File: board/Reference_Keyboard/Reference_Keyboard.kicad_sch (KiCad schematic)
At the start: 76 parts, among them J1 Conn_01x03_Pin, J2 USB_C_Receptacle_USB2.0, J3 Conn_01x04_Pin, J4 84953-4, SW1 SW_Push, SW10 SW_Push, SW11 SW_Push, SW12 SW_Push, SW13 SW_Push, SW14 SW_Push, SW15 SW_Push, SW16 SW_Push, SW17 SW_Push, SW18 SW_Push, SW19 SW_Push, SW2 SW_Push, SW20 SW_Push, SW21 SW_Push, SW22 SKQGAFE010, SW23 SKQGAFE010, SW24 RotaryEncoder_Switch, SW3 SW_Push, SW4 SW_Push, SW5 SW_Push, SW6 SW_Push, SW7 SW_Push, SW8 SW_Push, SW9 SW_Push, U1 RP2040, U2 W25Q16JVSSIM, U3 LM1117RS-3.3, Y1 NX3225SA-12MHz-STD-CSR-6

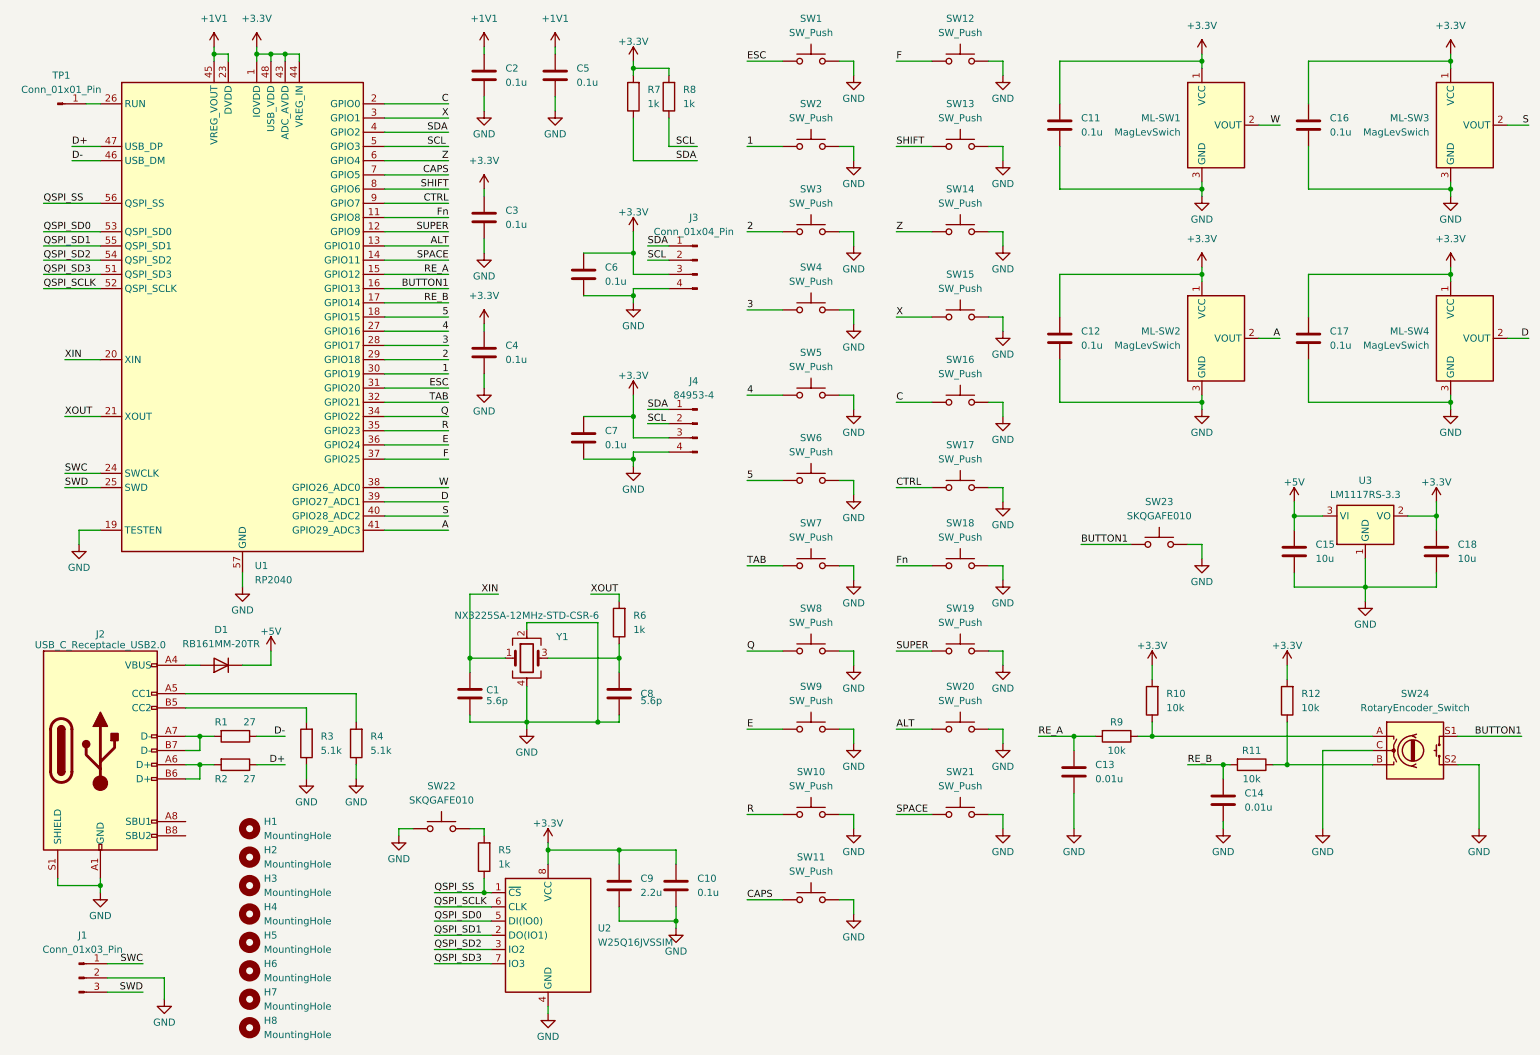
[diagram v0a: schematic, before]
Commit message: add firmware and PCB for hardware v1.01
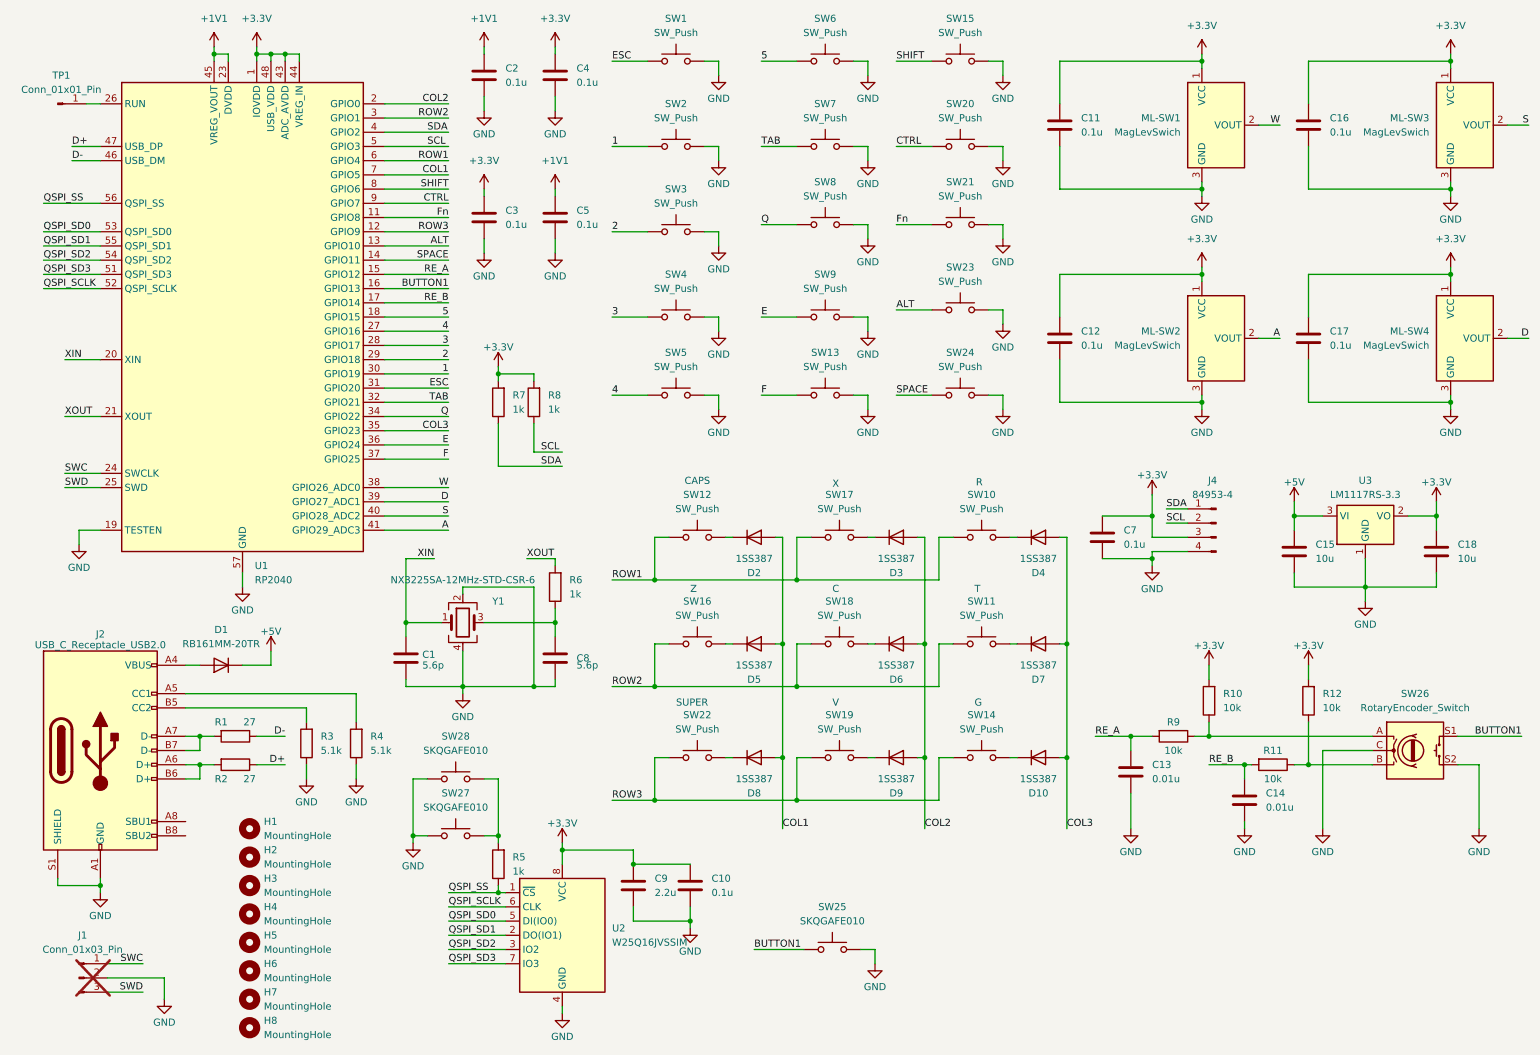
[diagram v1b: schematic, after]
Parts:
- removed C6: 0.1u, Capacitor_SMD:C_0603_1608Metric, symbol Device:C
- removed J3: Conn_01x04_Pin, Connector_PinHeader_2.54mm:PinHeader_1x04_P2.54mm_Vertical, symbol Connector:Conn_01x04_Pin
- added D10, D2, D3, D4, D5, D6, D7, D8, D9: 1SS387, Diode_SMD:D_SOD-523, symbol Device:D
- added SW12: SW_Push, MX_Hotswap:MX-Hotswap-1.75U, symbol Switch:SW_Push
- added SW14, SW22: SW_Push, MX_Hotswap:MX-Hotswap-1U, symbol Switch:SW_Push
- added SW28: SKQGAFE010, Button_Switch_SMD:SW_SPST_SKQG_WithStem, symbol Switch:SW_Push
- J1: now not fitted
- SW11: footprint MX_Hotswap:MX-Hotswap-1.75U -> MX_Hotswap:MX-Hotswap-1U
- renumbered SW12 to SW13, SW13 to SW15, SW14 to SW16, SW15 to SW17, SW16 to SW18, SW17 to SW20, SW18 to SW21, SW20 to SW23, SW21 to SW24, SW23 to SW25, SW24 to SW26, SW22 to SW27
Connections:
- net GND: now also SW28.1; no longer SW10.2, SW11.2, SW16.2, SW17.2, SW18.2, SW19.2
- net at R5.2, SW27.2: now also SW28.2
- net C renamed COL2
- net COL2: now also D3.2 (A), D6.2 (A), D9.2 (A); no longer SW18.1
- net CAPS renamed COL1
- net COL1: now also D2.2 (A), D5.2 (A), D8.2 (A); no longer SW11.1
- net R renamed COL3
- net COL3: now also D10.2 (A), D4.2 (A), D7.2 (A); no longer SW10.1
- net SUPER renamed ROW3
- net ROW3: now also SW14.1, SW22.1
- net X renamed ROW1
- net ROW1: now also SW10.1, U1.6 (GPIO4), SW12.1; no longer U1.3 (GPIO1)
- net Z renamed ROW2
- net ROW2: now also SW11.1, SW18.1, U1.3 (GPIO1); no longer U1.6 (GPIO4)
- new net: D4.1 (K), SW10.2
- new net: D2.1 (K), SW12.2
- new net: D8.1 (K), SW22.2
- new net: D9.1 (K), SW19.2
- new net: D6.1 (K), SW18.2
- new net: D5.1 (K), SW16.2
- new net: D3.1 (K), SW17.2
- new net: D7.1 (K), SW11.2
- new net: D10.1 (K), SW14.2
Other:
- note added: "C"
- note added: "CAPS"
- note added: "G"
- note added: "R"
- note added: "SUPER"
- note added: "T"
- note added: "V"
- note added: "X"
- note added: "Z"
- moved on the sheet: C1, C10, C13, C14, C4, C5, C7, C8, C9, J4, R10, R11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
